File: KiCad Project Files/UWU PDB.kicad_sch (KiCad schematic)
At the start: 73 parts, among them J1 XT90, J10 XT60 ESC, J11 PWM ESC, J12 PWM ESC, J13 PWM ESC, J14 PWM ESC, J15 PWM ESC, J16 PWM ESC, J17 PWM ESC, J18 PWM ESC, J19 XT90, J2 Conn_02x08_Odd_Even, J3 XT60 ESC, J4 XT60 ESC, J5 XT60 ESC, J6 XT60 ESC, J7 XT60 ESC, J8 XT60 ESC, J9 XT60 ESC

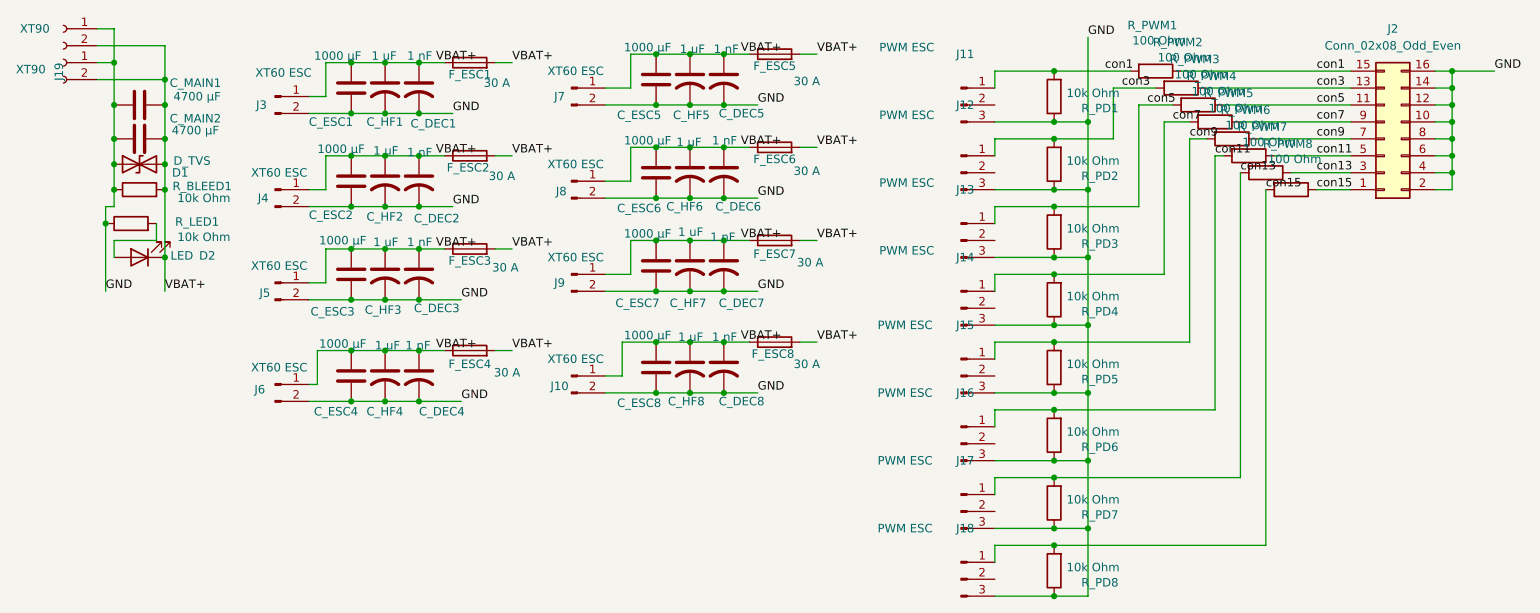
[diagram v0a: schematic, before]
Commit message: Update KiCad design files and refresh screenshots
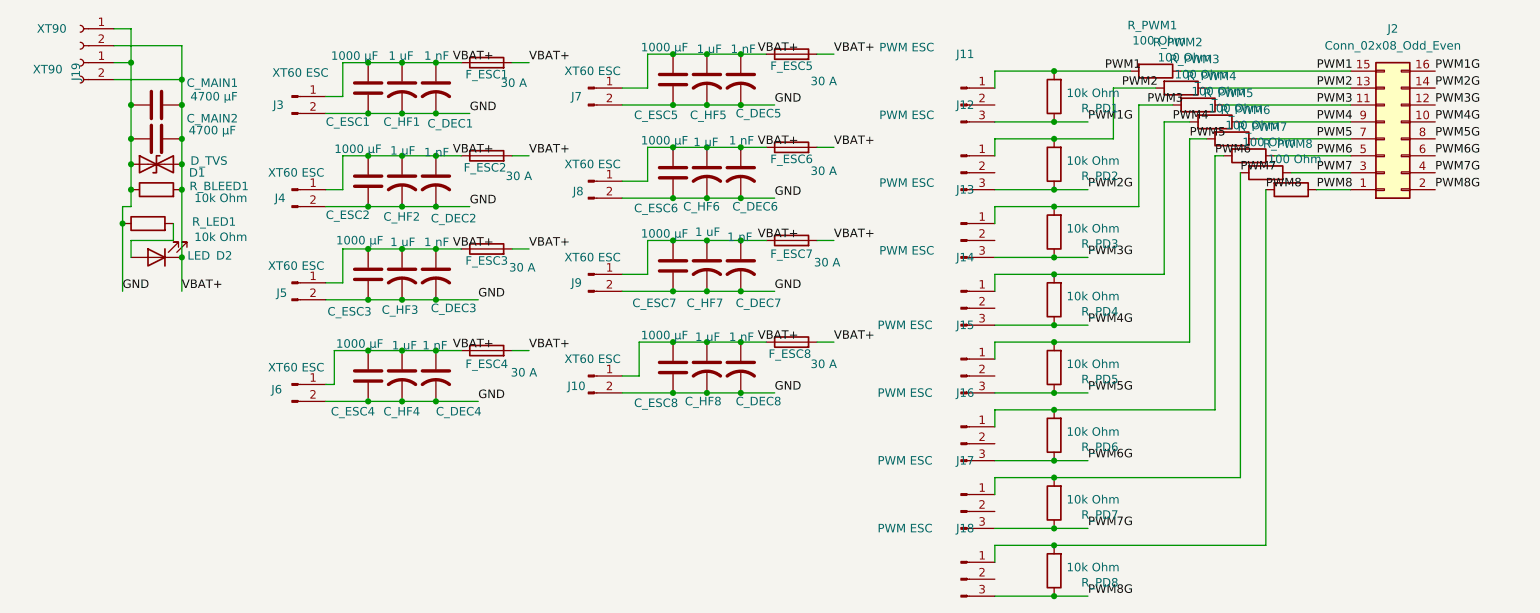
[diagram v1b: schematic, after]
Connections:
- net GND: no longer J11.3 (Pin_3), J12.3 (Pin_3), J13.3 (Pin_3), J14.3 (Pin_3), J15.3 (Pin_3), J16.3 (Pin_3), J17.3 (Pin_3), J18.3 (Pin_3), J2.10 (Pin_10), J2.12 (Pin_12), J2.14 (Pin_14), J2.16 (Pin_16), J2.2 (Pin_2), J2.4 (Pin_4), J2.6 (Pin_6), J2.8 (Pin_8), R_PD1.1, R_PD2.1, R_PD3.1, R_PD4.1, R_PD5.1, R_PD6.1, R_PD7.1, R_PD8.1
- net con1 renamed PWM1
- net con11 renamed PWM6
- net con13 renamed PWM7
- net con15 renamed PWM8
- net con3 renamed PWM2
- net con5 renamed PWM3
- net con7 renamed PWM4
- net con9 renamed PWM5
- new net PWM1G: J11.3 (Pin_3), J2.16 (Pin_16), R_PD1.1
- new net PWM2G: J12.3 (Pin_3), J2.14 (Pin_14), R_PD2.1
- new net PWM3G: J13.3 (Pin_3), J2.12 (Pin_12), R_PD3.1
- new net PWM4G: J14.3 (Pin_3), J2.10 (Pin_10), R_PD4.1
- new net PWM5G: J15.3 (Pin_3), J2.8 (Pin_8), R_PD5.1
- new net PWM6G: J16.3 (Pin_3), J2.6 (Pin_6), R_PD6.1
- new net PWM7G: J17.3 (Pin_3), J2.4 (Pin_4), R_PD7.1
- new net PWM8G: J18.3 (Pin_3), J2.2 (Pin_2), R_PD8.1
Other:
- moved on the sheet: C_DEC1, C_DEC2, C_DEC3, C_DEC4, C_DEC5, C_DEC6, C_DEC7, C_DEC8, C_ESC1, C_ESC2, C_ESC3, C_ESC4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
